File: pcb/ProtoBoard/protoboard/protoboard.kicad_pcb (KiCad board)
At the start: 2 copper layers, 50 x 50 mm, 3 parts, among them J1 I2C1, U2 Pololu_Breakout_DRV8874, U3 Pololu_Breakout_DRV8874

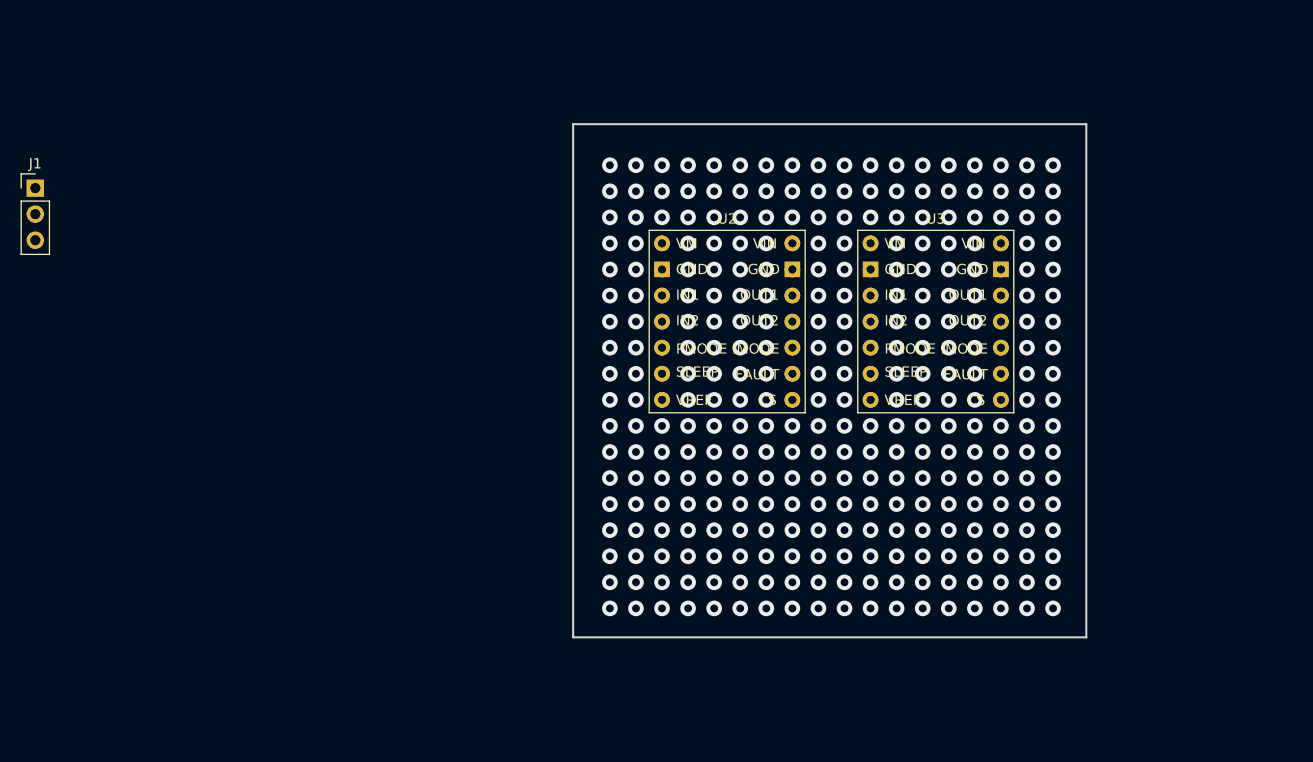
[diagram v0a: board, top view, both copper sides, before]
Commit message: started perfboard layout
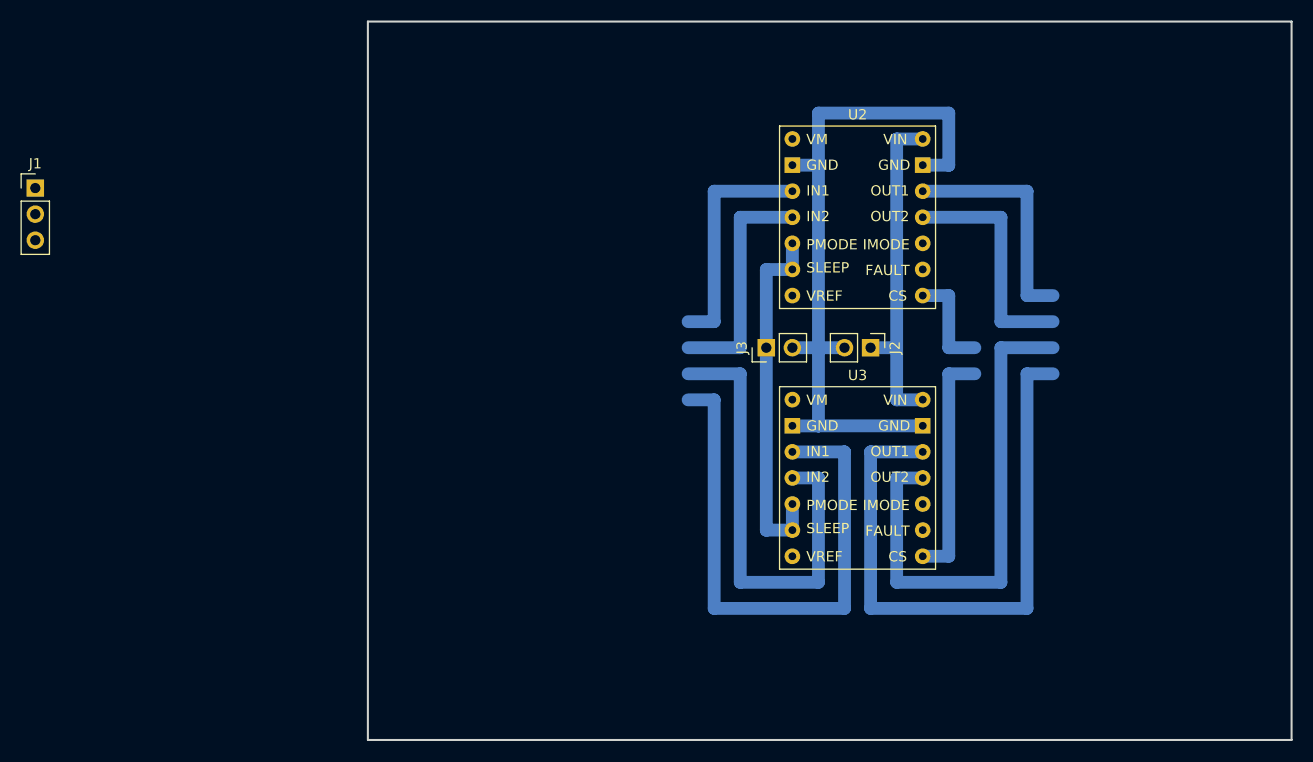
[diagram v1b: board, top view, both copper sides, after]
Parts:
- added J2: 24V Power, Connector_PinHeader_2.54mm:PinHeader_1x02_P2.54mm_Vertical, F.Cu at (157.5, 68.6)
- added J3: USB Power, Connector_PinHeader_2.54mm:PinHeader_1x02_P2.54mm_Vertical, F.Cu at (147.3, 68.6)
- moved U3 17.0 mm to (156.2, 81.3)
- moved U2 16.3 mm to (156.2, 55.9)
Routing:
- net AGND: track 0.00 -> 71.1 mm, vias 9 -> 0
- net /Phase B+: track 0.00 -> 61.0 mm, vias 1 -> 0
- net /IN1_B+: track 0.00 -> 55.9 mm, vias 1 -> 0
- net /Phase B-: track 0.00 -> 50.8 mm, vias 1 -> 0
- net /IN2_B-: track 0.00 -> 45.7 mm, vias 1 -> 0
- net +3.3V: track 0.00 -> 35.6 mm, vias 6 -> 0
- net +24V: track 0.00 -> 33.0 mm, vias 5 -> 0
- net /IN1_A+: track 0.00 -> 22.9 mm, vias 3 -> 0
- net /IN2_A-: track 0.00 -> 22.9 mm, vias 2 -> 0
- net /Phase A-: track 0.00 -> 22.9 mm, vias 2 -> 0
- net /Phase A+: track 0.00 -> 22.9 mm, vias 2 -> 0
- net /Phase_B_CS: track 0.00 -> 22.9 mm, vias 1 -> 0
- net /Phase_A_CS: track 0.00 -> 10.2 mm, vias 4 -> 0
- net unconnected-(U3-VREF-Pad7): vias 1 -> 0
- net unconnected-(U3-IMODE-Pad12): vias 1 -> 0
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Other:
- board size 50 x 50 mm -> 90 x 70 mm

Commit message: changed spi variable
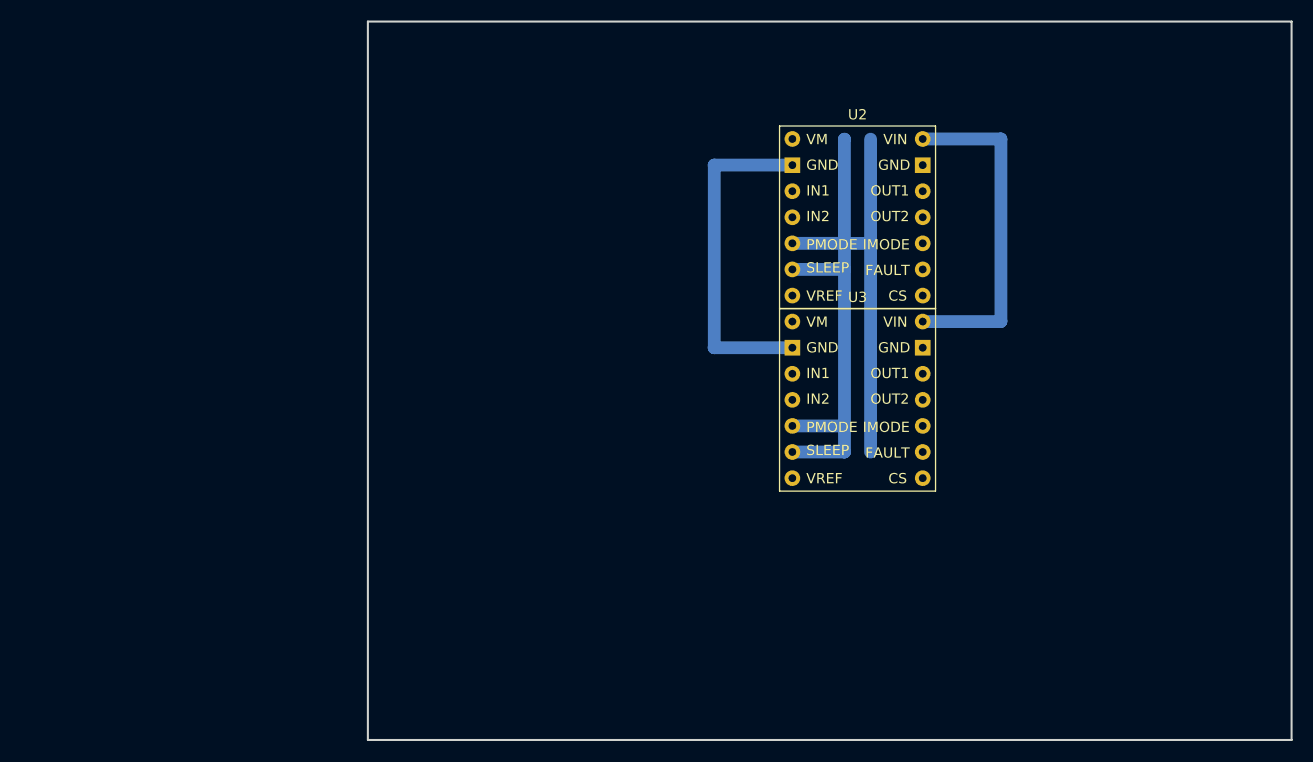
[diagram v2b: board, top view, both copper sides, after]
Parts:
- removed J1: I2C1, Connector_PinHeader_2.54mm:PinHeader_1x03_P2.54mm_Vertical
- removed J2: 24V Power, Connector_PinHeader_2.54mm:PinHeader_1x02_P2.54mm_Vertical
- removed J3: USB Power, Connector_PinHeader_2.54mm:PinHeader_1x02_P2.54mm_Vertical
- moved U3 7.61 mm to (156.2, 73.7)
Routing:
- net /Phase B+: track 61.0 -> 0.00 mm
- net /IN1_B+: track 55.9 -> 0.00 mm
- net /Phase B-: track 50.8 -> 0.03 mm
- net +3.3V: track 35.6 -> 83.8 mm
- net /IN2_B-: track 45.7 -> 0.00 mm
- net AGND: track 71.1 -> 33.0 mm
- net /IN1_A+: track 22.9 -> 0.00 mm
- net /IN2_A-: track 22.9 -> 0.00 mm
- net /Phase A-: track 22.9 -> 0.00 mm
- net /Phase A+: track 22.9 -> 0.00 mm
- net /Phase_B_CS: track 22.9 -> 0.00 mm
- net /Phase_A_CS: track 10.2 -> 0.00 mm
